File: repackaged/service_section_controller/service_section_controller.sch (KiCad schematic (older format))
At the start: 0 parts

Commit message: Add files via upload
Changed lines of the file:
@@
 $Descr A4 11693 8268
 encoding utf-8
-Sheet 1 10
+Sheet 1 11
 Title ""
 Date ""
@@
 F1 "micros.sch" 50
 $EndSheet
+$Sheet
+S 750  5800 2150 300
+U 60AEF08C
+F0 "shutdown" 50
+F1 "shutdown.sch" 50
+$EndSheet
 $EndSCHEMATC

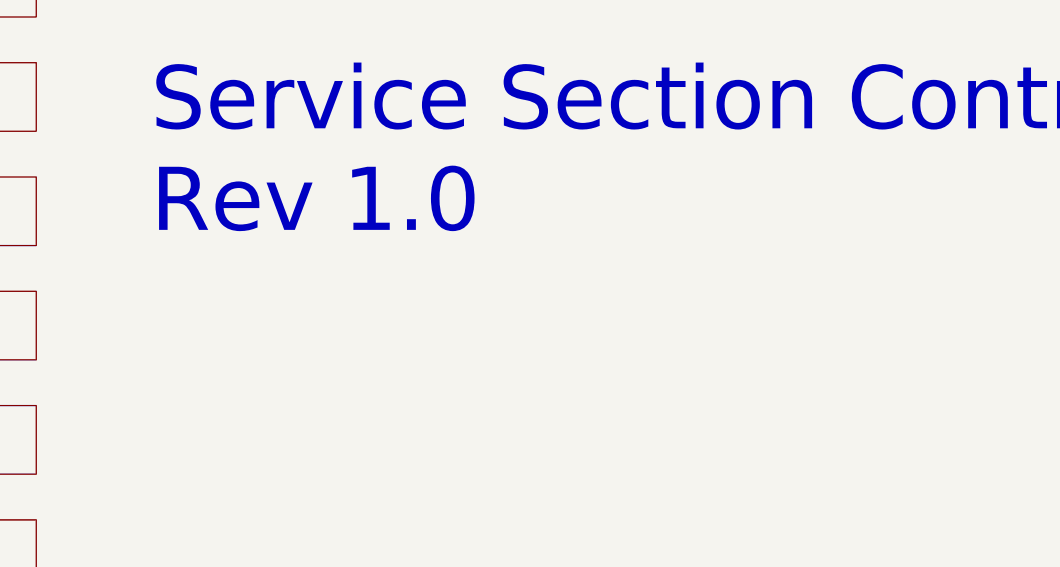
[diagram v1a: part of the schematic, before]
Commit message: added test points and re-did schematic with new traces.
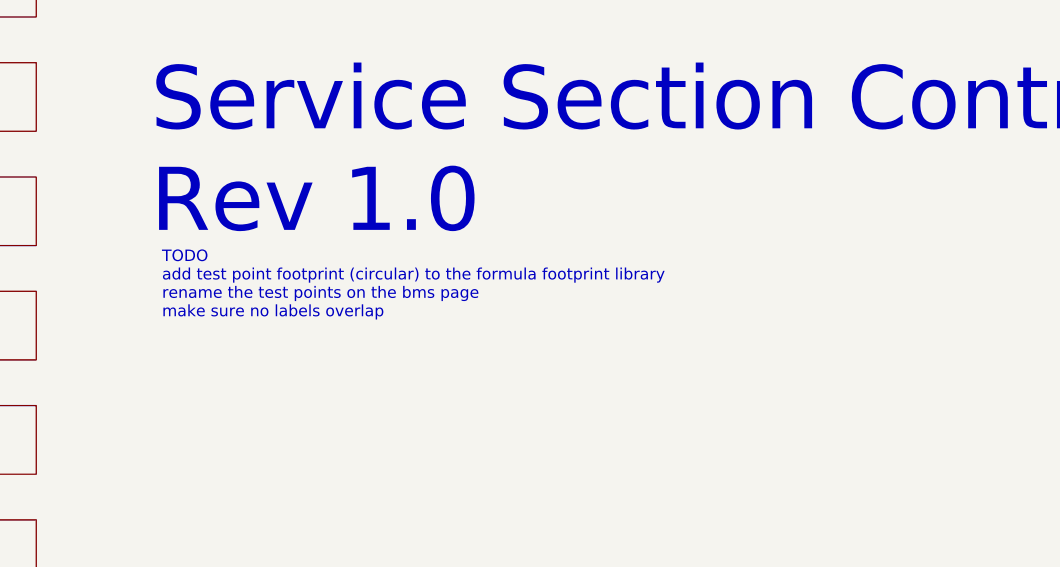
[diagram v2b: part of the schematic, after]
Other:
- note added: "TODO\nadd test point footprint (circular) to the formula footprint library\nrename the test points on the bms page \nmake sure no labels overlap"
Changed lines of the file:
@@
 F1 "shutdown.sch" 50
 $EndSheet
+Text Notes 3450 4400 0    50   ~ 0
+TODO\nadd test point footprint (circular) to the formula footprint library\nrename the test points on the bms page \nmake sure no labels overlap
 $EndSCHEMATC
